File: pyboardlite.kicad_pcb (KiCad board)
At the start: 2 copper layers, 27 parts, among them J1 USB_OTG, J2 Conn_02x03_Top_Bottom, SW1 Button-PTM, U1 LP2980AIM5-3.3, U2 STM32F405RGT6, Y1 8MHz

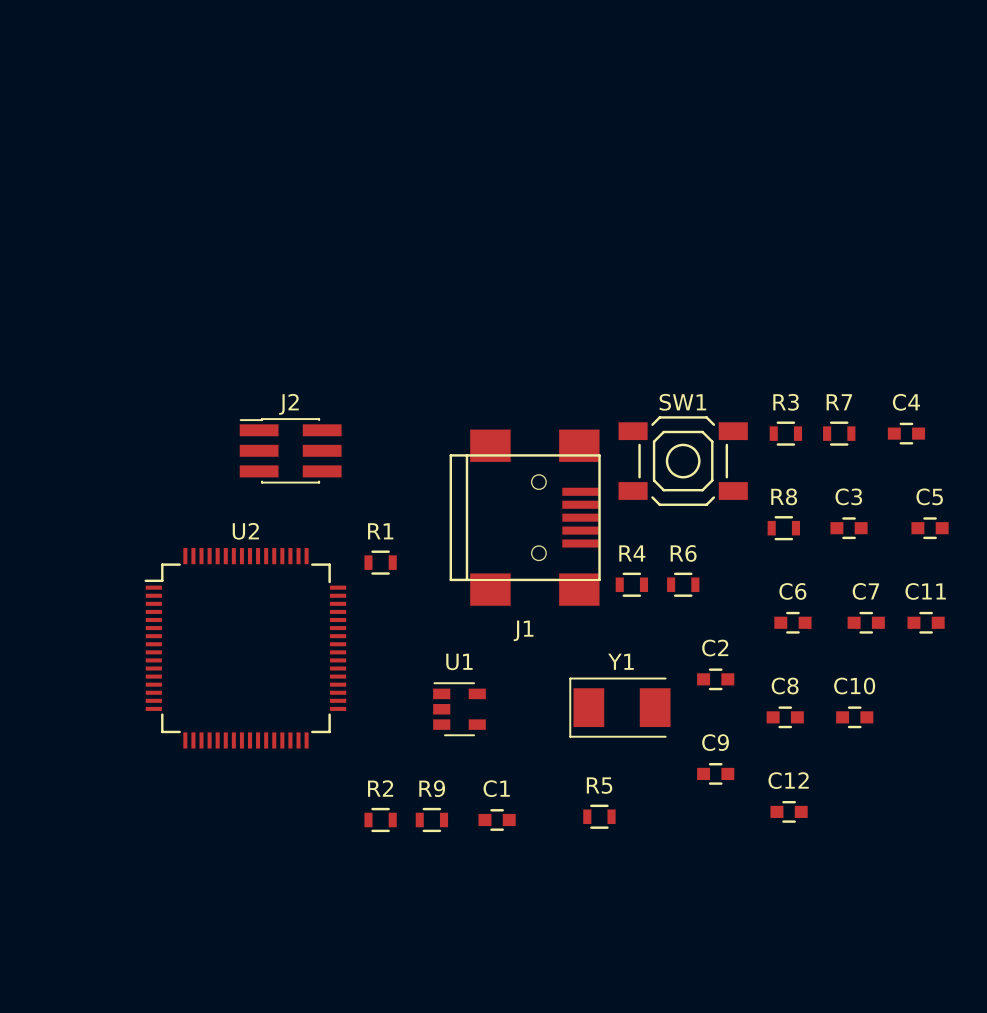
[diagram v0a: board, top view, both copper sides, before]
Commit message: Swapping SWD header pin order
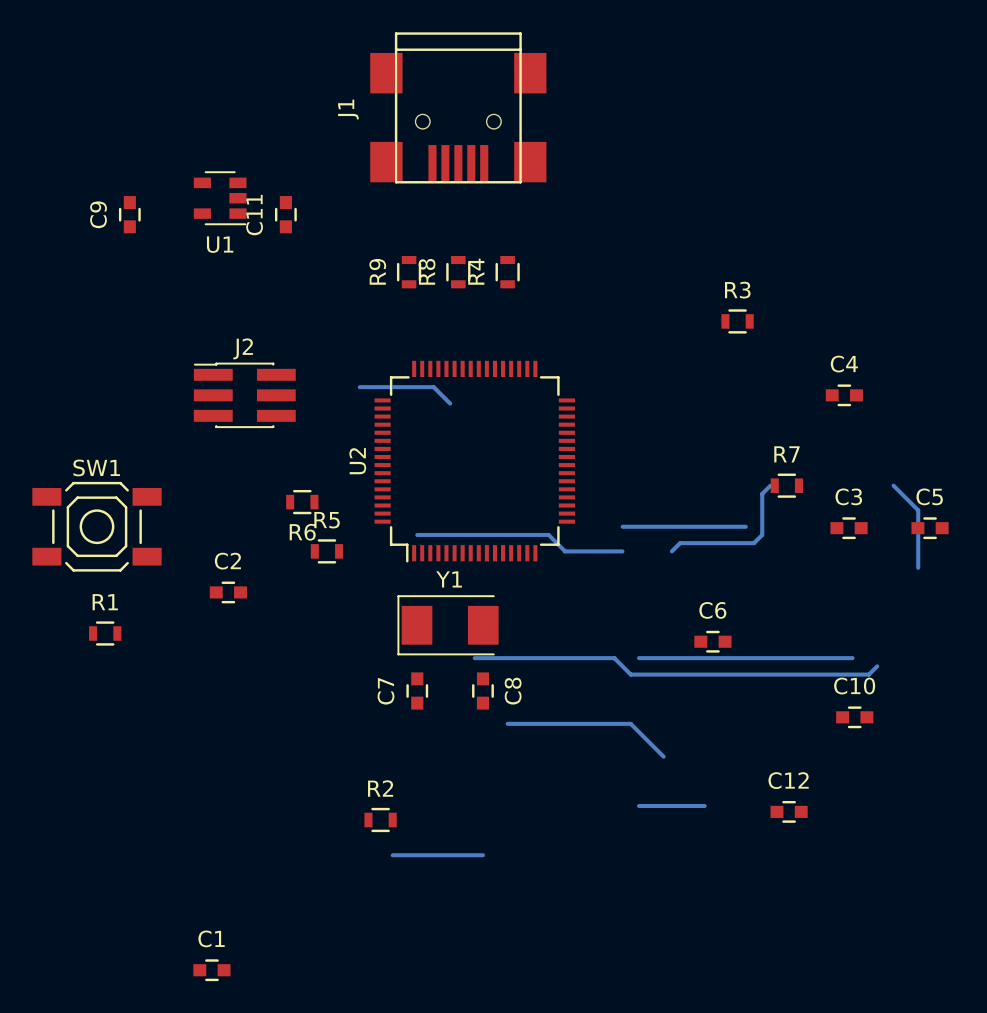
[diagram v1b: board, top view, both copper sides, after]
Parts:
- J2: value Conn_02x03_Top_Bottom -> Conn_02x03_Odd_Even
- moved C9 50.1 mm to (192.0, 75.7), turned to 90 degrees
- moved C11 47.0 mm to (201.7, 75.7), turned to 90 degrees
- moved SW1 36.5 mm to (190.0, 95.0)
- moved U1 34.9 mm to (197.6, 74.7), turned to 180 degrees
- moved R9 33.9 mm to (209.3, 79.2), turned to 90 degrees
- moved C2 30.6 mm to (198.1, 99.1)
- moved C7 28.1 mm to (209.8, 105.2), turned to 90 degrees
- moved J1 25.7 mm to (212.3, 69.1), turned to 270 degrees
- moved R8 25.6 mm to (212.3, 79.2), turned to 90 degrees
- moved R6 24.1 mm to (202.7, 93.5), turned to 180 degrees
- moved R5 23.5 mm to (204.2, 96.5)
- moved R4 20.8 mm to (215.4, 79.2), turned to 90 degrees
- moved C1 19.9 mm to (197.1, 122.4)
- moved C8 18.8 mm to (213.9, 105.2), turned to 270 degrees
- moved U2 18.3 mm to (213.4, 90.9), turned to 90 degrees
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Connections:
- J2 pad 2: GND -> /SWDIO
- J2 pad 3: Net-(J2-Pad3) -> GND
- J2 pad 5: /SWDIO -> Net-(J2-Pad5)
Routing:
- net (no net): track 0.00 -> 100.6 mm

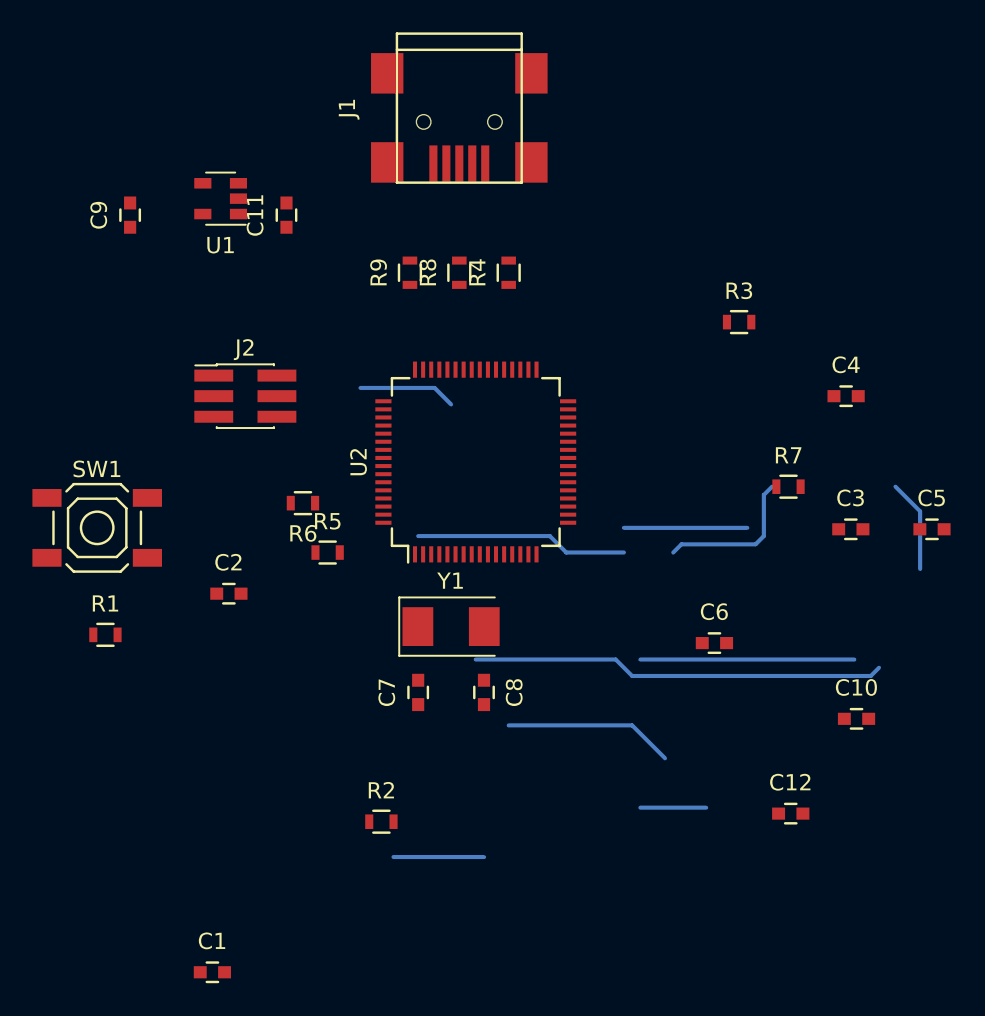
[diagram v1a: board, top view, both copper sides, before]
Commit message: Added LED, did initial board placement and track routing.
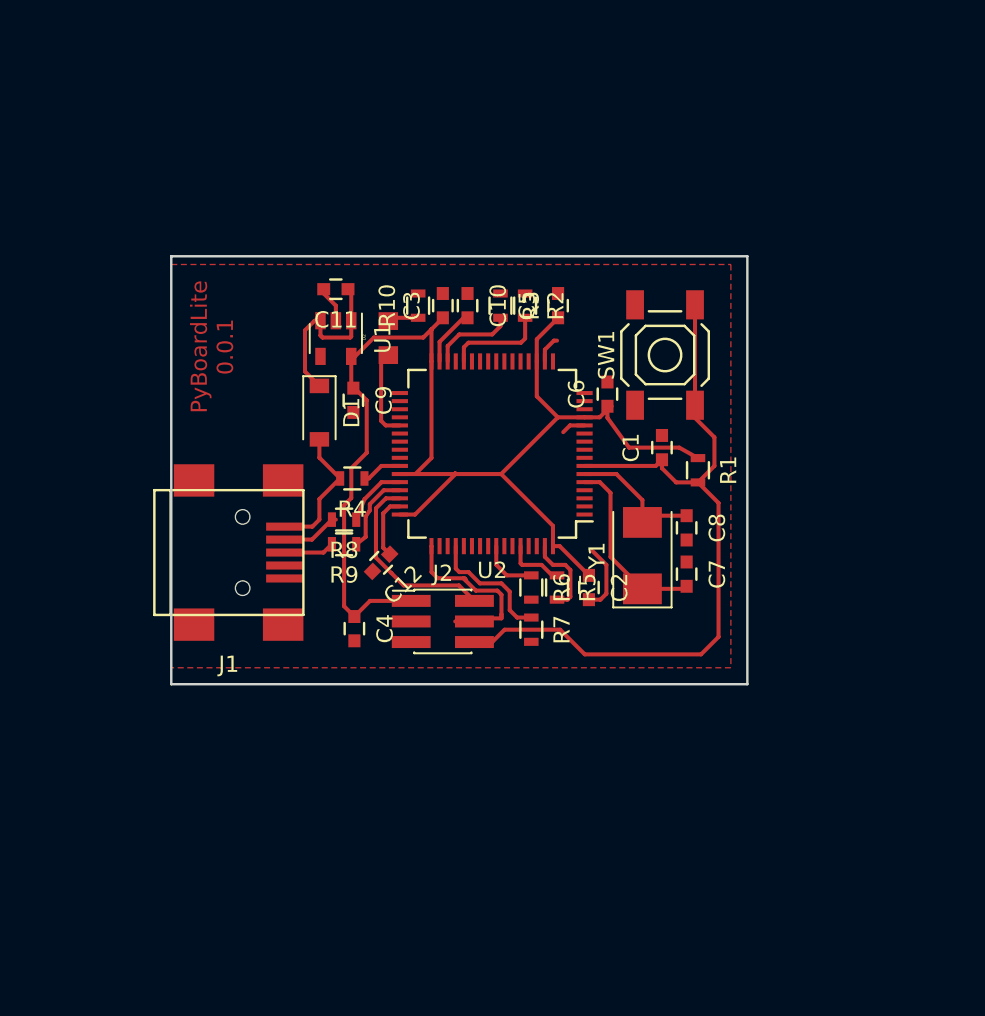
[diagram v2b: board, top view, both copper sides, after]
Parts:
- added D1: D_Schottky, Diodes_SMD:D_SOD-123, F.Cu at (203.7, 87.9)
- added D2: LED_Small, custom:150080GS75000, F.Cu at (208.0, 82.2)
- added R10: 1K, Resistors_SMD:R_0603, F.Cu at (209.8, 81.3)
- moved C1 42.6 mm to (224.9, 90.0), turned to 90 degrees
- moved R1 38.0 mm to (227.1, 91.4), turned to 270 degrees
- moved SW1 36.6 mm to (225.0, 84.3), turned to 90 degrees
- moved C10 35.0 mm to (212.9, 81.3), turned to 270 degrees
- moved C4 33.6 mm to (205.9, 101.2), turned to 270 degrees
- moved R2 33.1 mm to (216.4, 81.3), turned to 270 degrees
- moved J1 30.9 mm to (198.1, 96.5), turned to 0 degrees
- moved C12 29.6 mm to (207.5, 97.2), turned to 225 degrees
- moved C3 28.7 mm to (211.3, 81.3), turned to 90 degrees
- moved C5 26.9 mm to (218.4, 81.3), turned to 90 degrees
- moved C2 22.2 mm to (220.3, 98.7), turned to 270 degrees
- moved J2 18.5 mm to (211.3, 100.8)
- moved R7 18.2 mm to (216.8, 101.3), turned to 270 degrees
- moved C7 18.1 mm to (226.4, 97.9), turned to 270 degrees
- moved C9 17.9 mm to (205.8, 87.1), turned to 270 degrees
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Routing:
- net (no net): track 100.6 -> 0.00 mm
- net +3V3: track 0.00 -> 80.2 mm
- net /NRST: track 0.00 -> 46.4 mm
- net GND: track 0.00 -> 14.8 mm
- net /SWDIO: track 0.00 -> 12.0 mm
- net Net-(C7-Pad2): track 0.00 -> 11.7 mm
- net /SWCLK: track 0.00 -> 11.0 mm
- net +5V: track 0.00 -> 10.9 mm
- net Net-(C8-Pad1): track 0.00 -> 9.55 mm
- net Net-(D1-Pad2): track 0.00 -> 8.34 mm
- net Net-(R7-Pad1): track 0.00 -> 7.97 mm
- net Net-(R2-Pad2): track 0.00 -> 6.16 mm
- net Net-(D2-Pad2): track 0.00 -> 5.97 mm
- net Net-(R3-Pad2): track 0.00 -> 5.23 mm
- net Net-(R9-Pad1): track 0.00 -> 5.06 mm
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- added copper zone on F.Cu, net GND
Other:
- board outline added: 35.6 x 26.4 mm
- board text added: "PyBoardLite 0.0.1"

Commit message: Jiggery pokery
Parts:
- added REF**: R_0603, Resistors_SMD:R_0603, F.Cu at (264.3, 46.9)
- added REF**: R_0603, Resistors_SMD:R_0603, F.Cu at (250.3, 43.8)
- moved R2 71.1 mm to (261.4, 26.2)
- moved R3 71.1 mm to (259.9, 26.2)
- moved R5 71.1 mm to (263.4, 43.6)
- moved C1 71.1 mm to (269.9, 35.0)
- moved C12 71.1 mm to (252.5, 42.1)
- moved C5 71.1 mm to (263.5, 26.2)
- moved C6 71.1 mm to (266.5, 31.7)
- moved D2 71.1 mm to (253.0, 27.2)
- moved R1 71.1 mm to (272.1, 36.4)
- moved R10 71.1 mm to (254.8, 26.2)
- moved R6 71.1 mm to (261.8, 43.6)
- moved C11 71.1 mm to (249.7, 25.2)
- moved C4 71.1 mm to (250.9, 46.2)
- moved C7 71.1 mm to (271.4, 42.8)
- moved C8 71.1 mm to (271.4, 39.9)
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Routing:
- net /SWCLK: track 11.0 -> 9.34 mm
- net GND: track 14.8 -> 16.4 mm

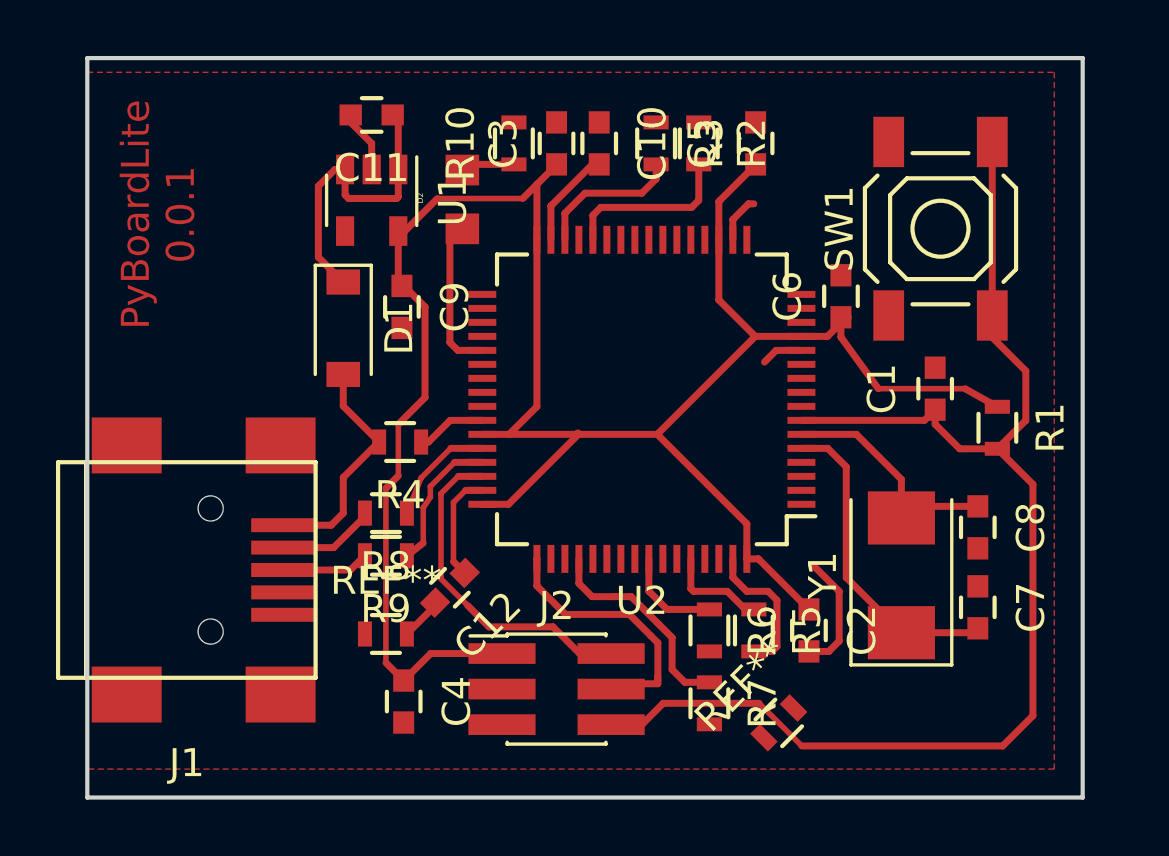
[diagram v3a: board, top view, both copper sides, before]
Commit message: Adding DFU jumper, moving a jumper resistor, enlarging the board slightly.
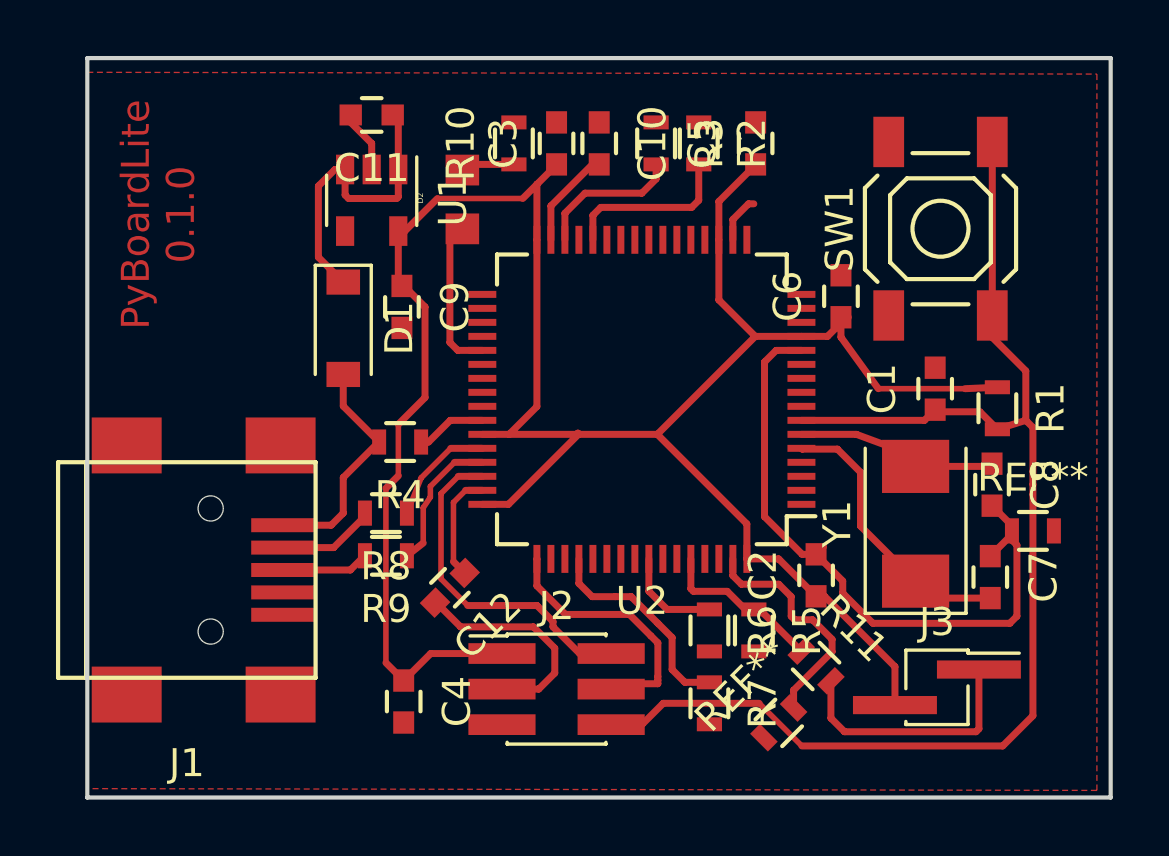
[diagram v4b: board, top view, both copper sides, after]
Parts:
- added J3: DFU_Jumper, Pin_Headers:Pin_Header_Straight_1x02_Pitch1.27mm_SMD_Pin1Right, F.Cu at (269.9, 45.7)
- added R11: 10K, Resistors_SMD:R_0603, F.Cu at (265.6, 44.9)
- moved REF** 23.4 mm to (273.4, 40.1)
- moved C2 1.98 mm to (265.6, 41.7), turned to 90 degrees
- moved Y1 1.91 mm to (269.2, 39.8)
- moved C8 1.61 mm to (271.9, 38.4)
- moved C7 1.17 mm to (271.8, 41.7)
- moved R1 0.70 mm to (272.1, 35.7)
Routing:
- net GND: track 16.4 -> 44.4 mm
- net Net-(J3-Pad1): track 0.00 -> 8.98 mm
- net +3V3: track 80.2 -> 85.3 mm
- net Net-(R11-Pad1): track 3.62 -> 5.93 mm
- net Net-(C7-Pad2): track 11.7 -> 10.4 mm
- net Net-(C8-Pad1): track 9.55 -> 8.97 mm
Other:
- board size 35.6 x 26.4 mm -> 36.6 x 26.4 mm
- board text added: "PyBoardLite 0.1.0"
- board text removed: "PyBoardLite 0.0.1"
